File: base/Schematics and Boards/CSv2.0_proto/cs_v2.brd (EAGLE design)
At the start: 38.1 x 44.5 mm, 80 parts, among them J101 J-JTAG-CORTEX-NEEDLE6-LEGS, J301 HIROSE-DF40_44-PIN_CONNECTORS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, J302 HIROSE-DF40_30-PIN_CONNECTORS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, Q201 FK3303010L, Q202 DMG3415UFY4Q-7, Q203 FK3303010L, Q204 FK3303010L, U101 ATSAMD51, U102 AT25SF641-MHB-T, U201 COULOMB-MAX17262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

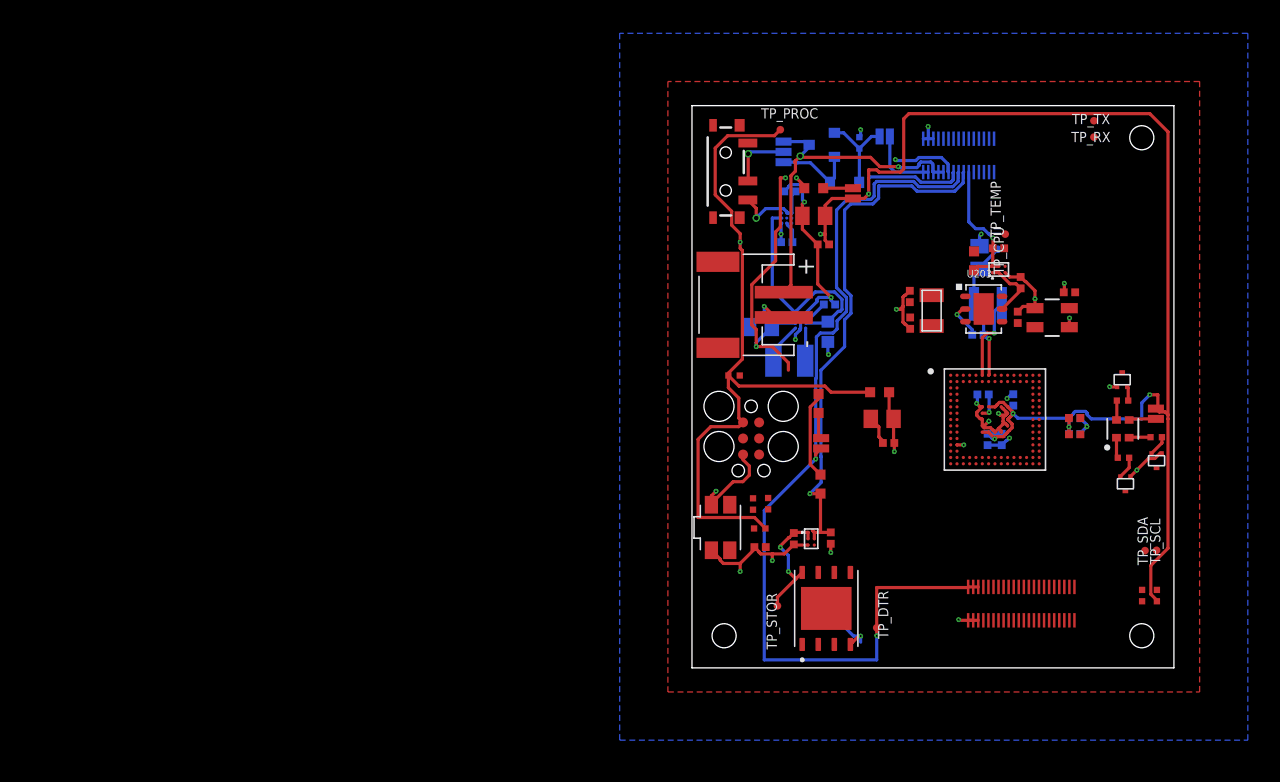
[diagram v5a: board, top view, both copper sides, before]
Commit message: Add screw holes (4) for M2 screws. Adjust layout and some traces
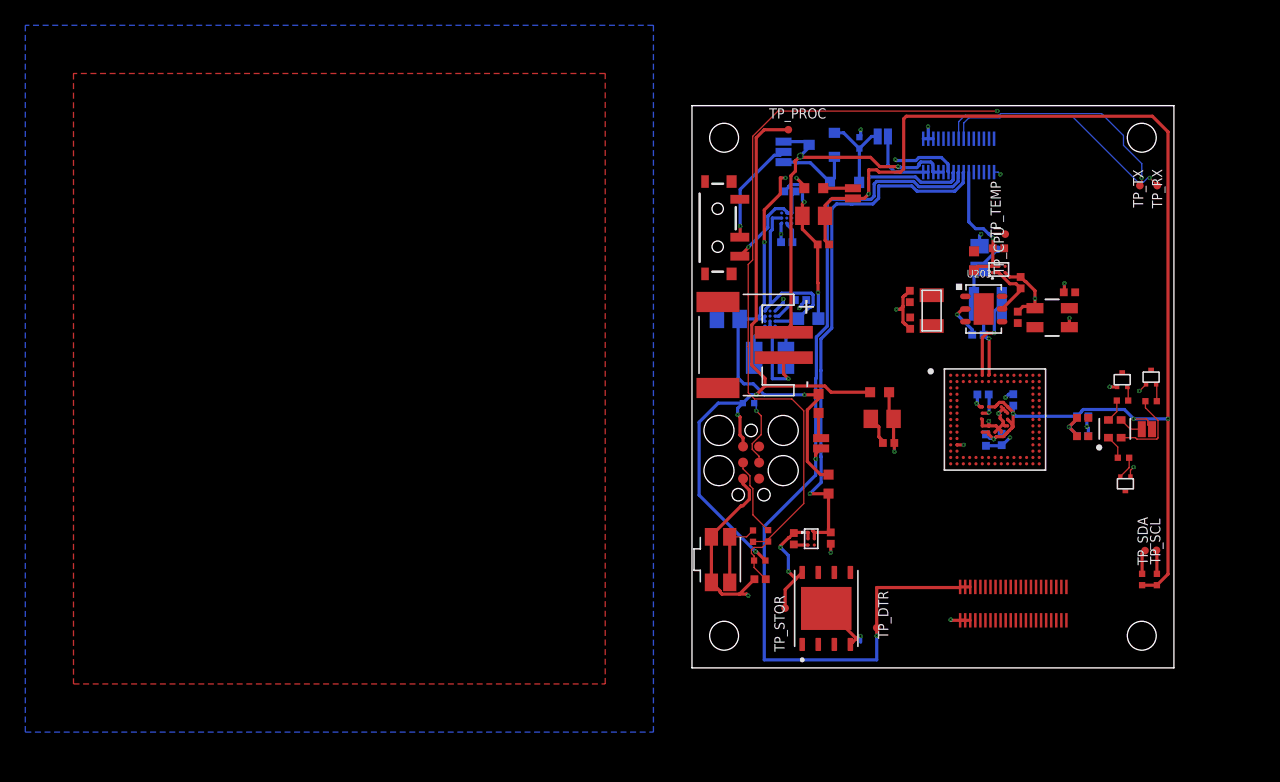
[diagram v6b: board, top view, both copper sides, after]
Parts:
- moved Q201 6.62 mm to (36.3, 23.0), turned to 0 degrees
- moved TP_RX 6.30 mm to (36.8, 38.1), turned to 90 degrees
- moved TP_TX 6.29 mm to (35.4, 38.1), turned to 180 degrees
- moved S201 4.49 mm to (2.03, 34.8)
- moved J201 3.18 mm to (3.56, 25.5)
- moved R202 2.87 mm to (36.3, 21.1)
- moved C205 2.62 mm to (2.87, 27.6)
- moved R101 2.54 mm to (5.36, 8.48)
- moved R102 2.54 mm to (4.83, 10.4)
- moved R105 2.54 mm to (6.02, 10.4)
- moved S101 2.54 mm to (2.26, 8.56)
- moved C101 2.54 mm to (5.38, 7.01)
- moved R106 2.47 mm to (4.47, 20.9), flipped to the bottom, turned to 0 degrees
- moved U202 2.42 mm to (6.17, 27.6)
- moved C204 2.31 mm to (8.59, 29.1)
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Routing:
- net NRESET: track 0.00 -> 68.3 mm, vias 0 -> 2
- net DBG_SERIAL_TX: track 0.00 -> 20.0 mm, vias 0 -> 1
- net DBG_SERIAL_RX: track 0.00 -> 19.3 mm, vias 0 -> 1
- net +3V3_PROC: track 176.4 -> 166.6 mm, vias 7 -> 9
- net JTAG_NRESET: track 0.00 -> 6.16 mm
- net N$5: track 0.00 -> 5.65 mm
- net DBG_SWCLK: track 0.00 -> 5.45 mm, vias 0 -> 1
- net +3V3: track 45.5 -> 50.1 mm, vias 4 -> 5
- net N$4: track 1.71 -> 6.32 mm
- net GND: track 86.0 -> 82.6 mm, vias 28 -> 27
- net VDD_SW_IN: track 5.02 -> 8.45 mm
- net +3V7_BATT: track 27.6 -> 30.7 mm
- net DTR_MASTER_I2C_SDA: track 0.00 -> 1.93 mm
- net DTR_MASTER_I2C_SCL: track 0.00 -> 1.87 mm
- net CC_IN: track 6.90 -> 8.29 mm
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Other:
- board text added: "Screw holes at 90 mil for M2 screws of ~79 mil diameter. M2 screw heads are approx 150 mil diameter. There must be appropriate space for this Standoff diameter should be <= 175mil. Wurth Electronik makes viable standoffs"
- board text removed: "Design needs screws, but must be v small #0 screws have 60 mil diameter. M1.6 may work (70 mil clearance) M0.6 screws also exist Added two place(hole)ders at 70 mils"

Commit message: Hand route a handful of signals to non-connector parts
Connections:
- net DBG_USB_D+ renamed DBG_USB_D_P
- net DBG_USB_D- renamed DBG_USB_D_N
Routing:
- net DTR_MASTER_I2C_SDA: track 1.93 -> 81.6 mm, vias 0 -> 7
- net DTR_MASTER_I2C_SCL: track 1.87 -> 80.1 mm, vias 0 -> 5
- net DBG_SWDIO: track 0.00 -> 69.0 mm, vias 0 -> 5
- net DBG_SWCLK: track 5.45 -> 68.6 mm, vias 1 -> 4
- net DTR_DETECT: track 0.00 -> 31.2 mm, vias 0 -> 2
- net LED_G: track 0.00 -> 20.4 mm, vias 0 -> 3
- net DBG_USB_D_P: track 0.00 -> 20.3 mm, vias 0 -> 1
- net DBG_USB_D_N: track 0.00 -> 19.8 mm, vias 0 -> 1
- net NRESET: track 68.3 -> 84.5 mm, vias 2 -> 3
- net EN_TEMP: track 0.00 -> 13.3 mm, vias 0 -> 2
- net LED_B: track 0.00 -> 10.8 mm, vias 0 -> 2
- net +3V3_PROC: track 166.6 -> 176.7 mm
- net LED_R: track 0.00 -> 10.0 mm, vias 0 -> 2
- net XIN: track 0.00 -> 9.89 mm
- net XIN32: track 0.00 -> 8.91 mm
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
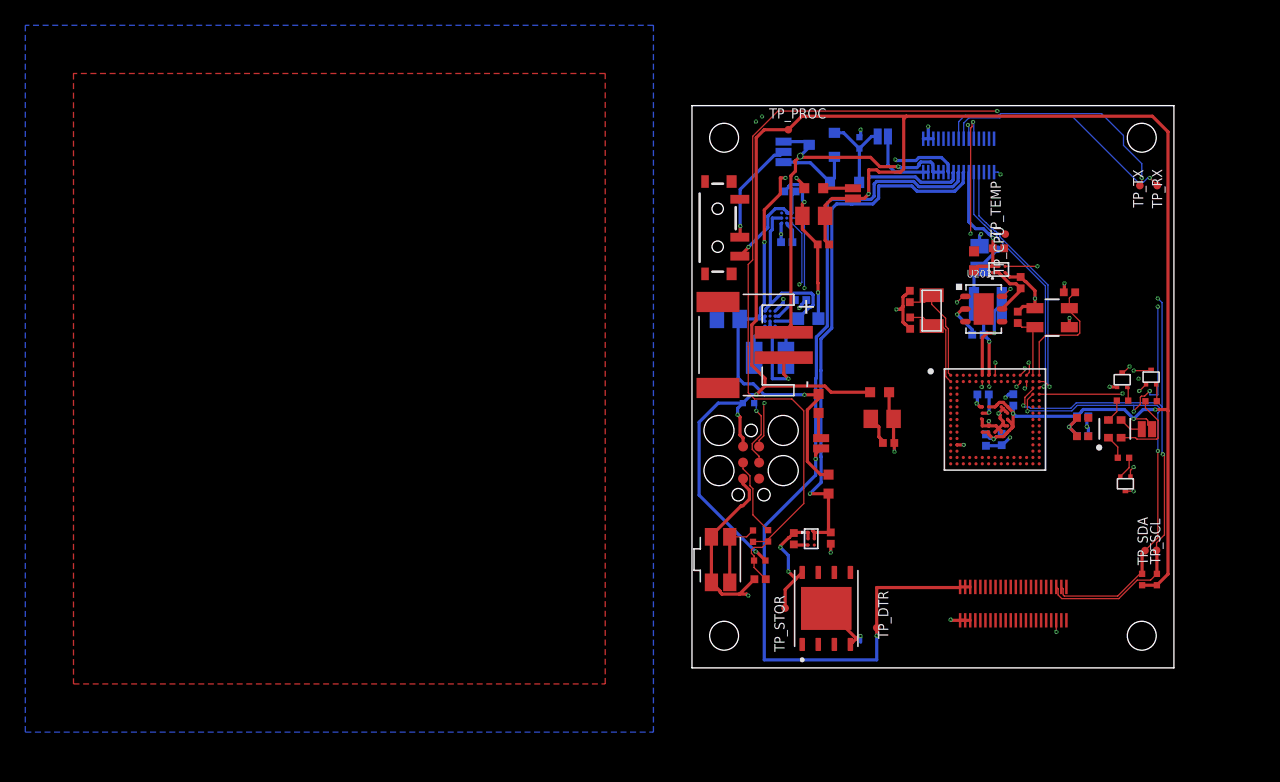
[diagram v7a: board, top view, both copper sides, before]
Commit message: Routed and GND-plugged
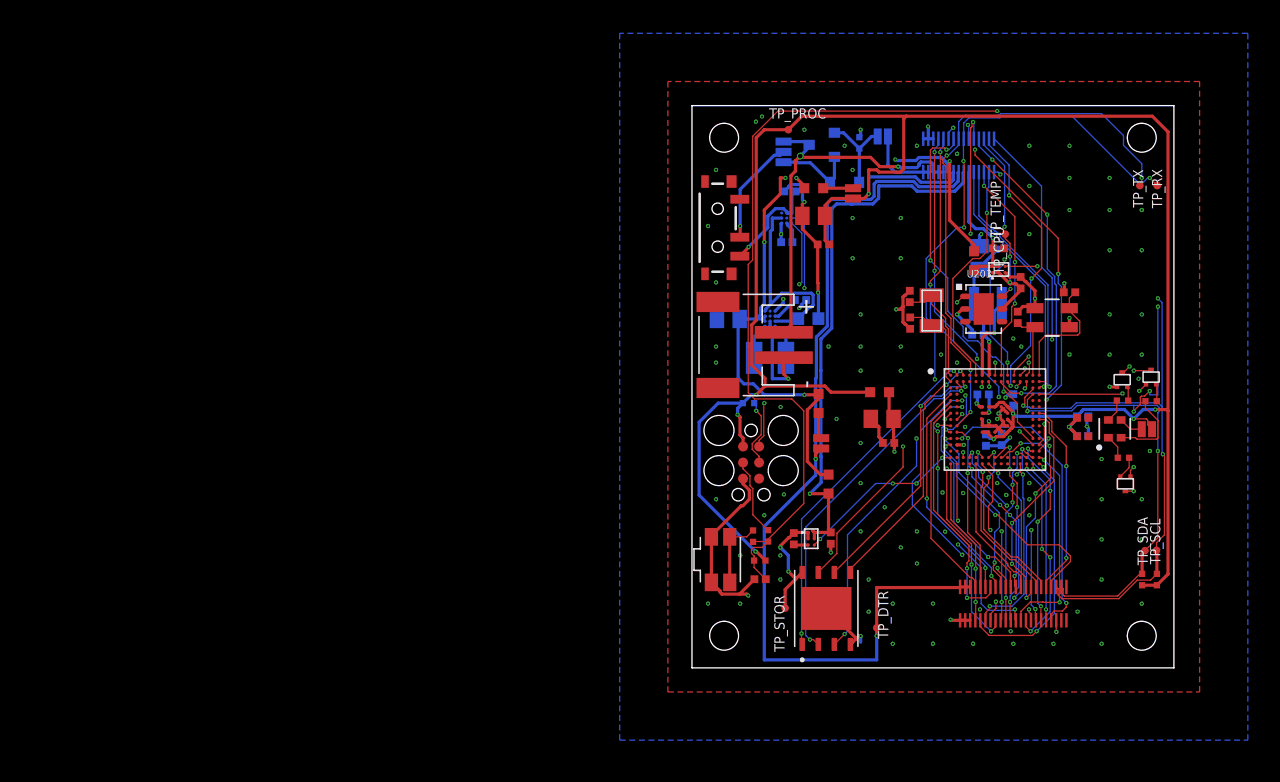
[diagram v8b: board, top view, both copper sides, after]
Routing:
- net DBG_GPIO2: track 0.00 -> 30.4 mm, vias 0 -> 5
- net DBG_GPIO3: track 0.00 -> 29.5 mm, vias 0 -> 3
- net DBG_GPIO0: track 0.00 -> 28.9 mm, vias 0 -> 4
- net DBG_GPIO1: track 0.00 -> 28.0 mm, vias 0 -> 4
- net DBG_SERIAL_RX: track 19.3 -> 47.3 mm, vias 1 -> 6
- net STOR_SPI5_MISO: track 0.00 -> 27.5 mm, vias 0 -> 2
- net STOR_SPI5_NCS: track 0.00 -> 27.3 mm, vias 0 -> 2
- net DBG_TRACE_D0: track 0.00 -> 27.1 mm, vias 0 -> 3
- net DBG_SERIAL_TX: track 20.0 -> 44.6 mm, vias 1 -> 4
- net STOR_WP: track 0.00 -> 24.0 mm, vias 0 -> 3
- net DBG_TRACE_D2: track 0.00 -> 22.7 mm, vias 0 -> 3
- net DTR_BUS3_GPIO0: track 0.00 -> 22.2 mm, vias 0 -> 4
- net DBG_TRACE_D3: track 0.00 -> 22.2 mm, vias 0 -> 2
- net DTR_BUS2_AIN1: track 0.00 -> 21.4 mm, vias 0 -> 3
- net STOR_SPI5_SCK: track 0.00 -> 20.6 mm, vias 0 -> 2
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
